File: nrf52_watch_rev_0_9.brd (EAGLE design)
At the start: 31 x 34 mm, 25 parts, among them IC1 HOLYIOT_18010, IC2 MX25R6435FM2IL0, IC4 MMA8652FCR1, J1 0528921033

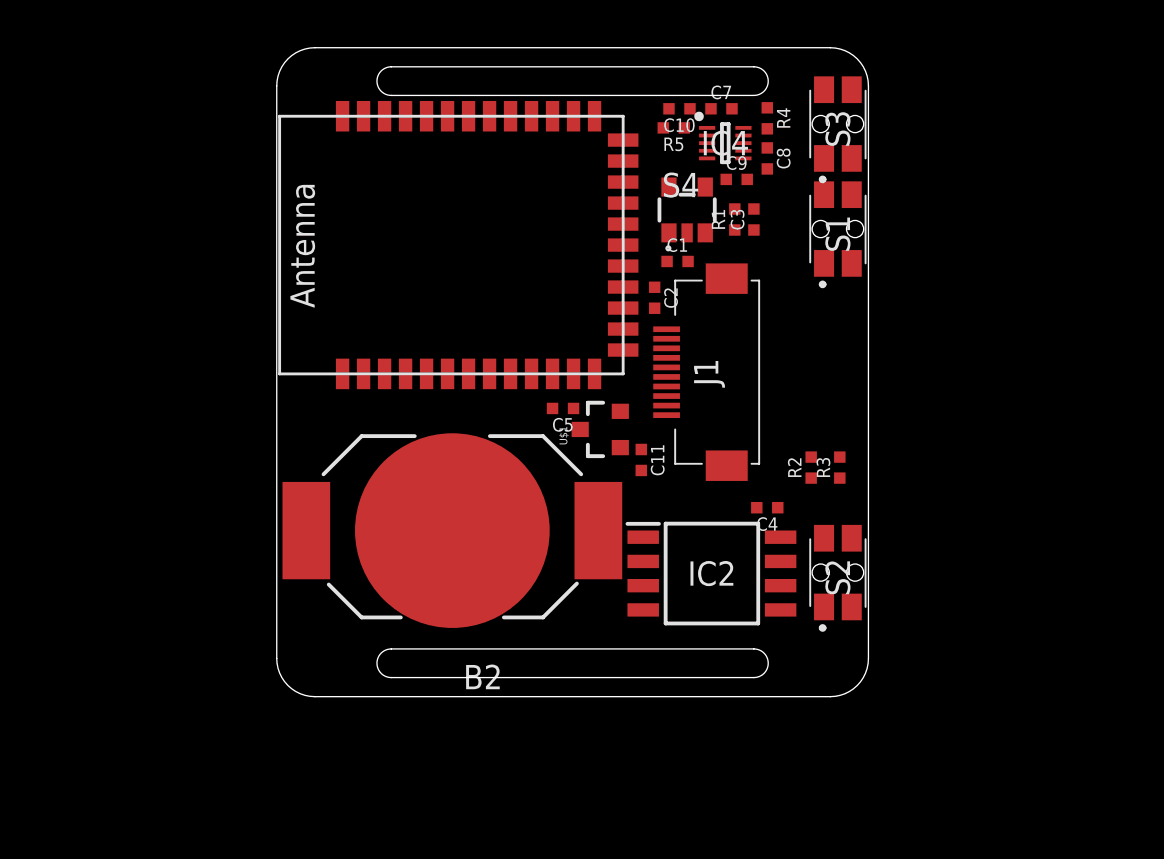
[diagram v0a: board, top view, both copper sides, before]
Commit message: first draft of routing done
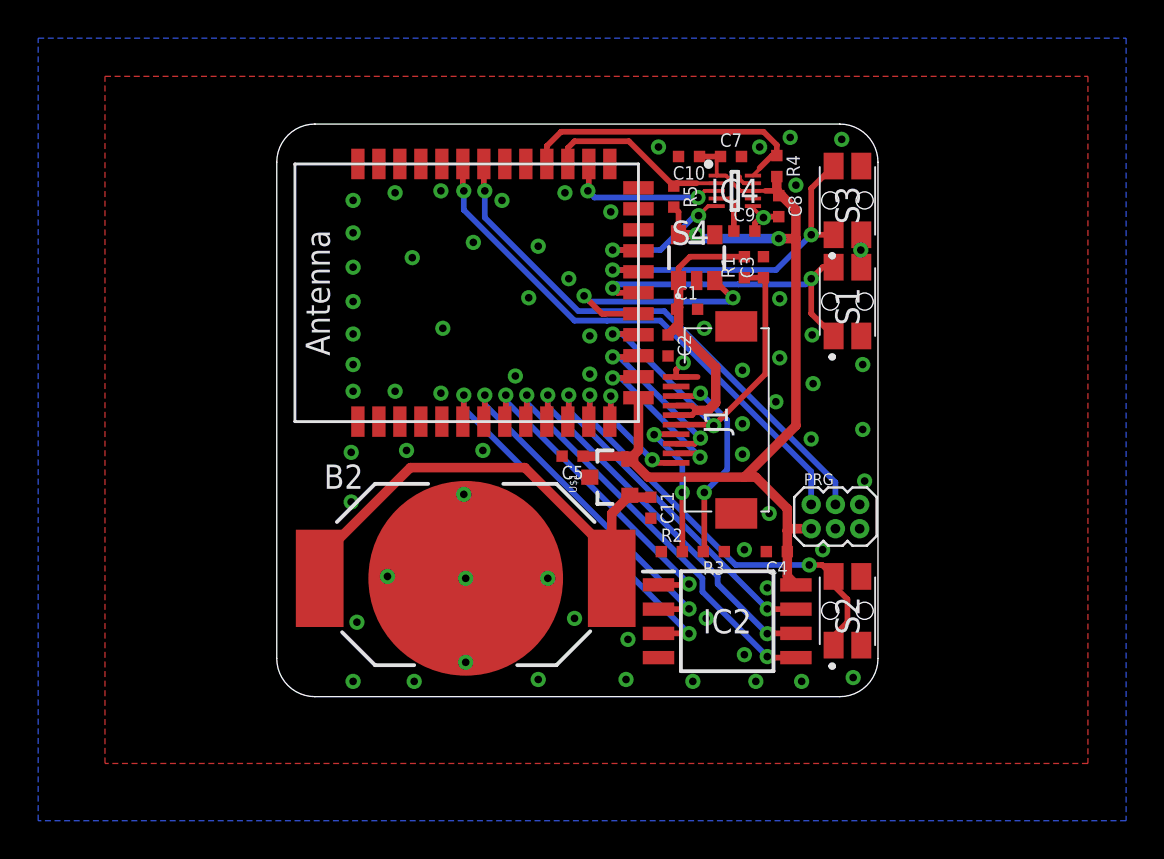
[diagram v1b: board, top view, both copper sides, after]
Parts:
- added PRG: NO_BOM, Inventas-Connectors:1X06_1.27MM
- moved R2 8.52 mm to (20.7, 7.60), turned to 0 degrees
- moved R3 7.93 mm to (22.9, 7.60), turned to 180 degrees
- moved S3 4.03 mm to (29.9, 26.0)
- moved S1 3.83 mm to (29.9, 20.7)
- moved R5 3.60 mm to (20.8, 26.2), turned to 270 degrees
- moved C9 2.73 mm to (24.5, 24.4)
- moved IC2 2.62 mm to (23.6, 3.95)
- moved IC1 2.62 mm to (9.95, 21.2)
- moved C2 2.60 mm to (20.5, 18.4)
- moved B2 2.60 mm to (9.90, 6.20)
- moved C8 2.57 mm to (26.3, 25.7)
- moved C1 2.55 mm to (21.5, 20.3)
- moved C10 2.55 mm to (21.6, 28.3)
- moved C11 2.55 mm to (19.6, 9.90)
- moved C3 2.55 mm to (25.5, 22.5)
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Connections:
- net ACC_INT1: now also IC1.26
- net ACC_INT2: now also IC1.21
- net BTN_BOTTOM: now also IC1.12
- net BTN_MID: now also IC1.19
- net BTN_TOP: now also IC1.20
- net GND: now also PRG.5
- net I2C_SCL: now also IC1.27
- net I2C_SDA: now also IC1.28
- net LCD_DISP: now also IC1.17
- net LCD_POWER_CONTROL: now also IC1.18
- net LCD_SCLK: now also IC1.13
- net LCD_SCS: now also IC1.16
- net LCD_SI: now also IC1.15
- net QSPI_CS: now also IC1.8
- net QSPI_SCLK: now also IC1.10
- net QSPI_SIO0: now also IC1.9
- net QSPI_SIO1: now also IC1.7
- net QSPI_SIO2: now also IC1.6
- net QSPI_SIO3: now also IC1.11
- net SWDCLK: now also PRG.4
- net SWDIO: now also PRG.2
- net VDD: now also PRG.1
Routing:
- net VDD: track 0.00 -> 51.6 mm, vias 0 -> 2
- net SWDCLK: track 0.00 -> 28.1 mm, vias 0 -> 1
- net SWDIO: track 0.00 -> 28.0 mm, vias 0 -> 1
- net N$1: track 0.00 -> 27.4 mm
- net BTN_BOTTOM: track 0.00 -> 23.1 mm, vias 0 -> 2
- net QSPI_SIO0: track 0.00 -> 21.9 mm, vias 0 -> 2
- net LCD_DISP: track 0.00 -> 20.6 mm, vias 0 -> 2
- net QSPI_SIO2: track 0.00 -> 20.4 mm, vias 0 -> 2
- net QSPI_SCLK: track 0.00 -> 20.2 mm, vias 0 -> 2
- net QSPI_SIO1: track 0.00 -> 18.6 mm, vias 0 -> 2
- net QSPI_SIO3: track 0.00 -> 18.4 mm, vias 0 -> 2
- net BTN_TOP: track 0.00 -> 17.8 mm, vias 0 -> 2
- net BTN_MID: track 0.00 -> 17.0 mm, vias 0 -> 2
- net QSPI_CS: track 0.00 -> 16.9 mm, vias 0 -> 2
- net LCD_POWER: track 0.00 -> 15.9 mm
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- added copper zone on layer 1, net GND
- added copper zone on layer 16, net GND
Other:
- board size 31 x 34 mm -> 31.5 x 30 mm

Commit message: changes to rouing. Added batter voltage measure. Added mounting holes
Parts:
- added C6: 10nF, Inventas-Passives:C0402
- added R7: 4M, Inventas-Passives:R0402
- added R8: 10M, Inventas-Passives:R0402
- moved C10 6.11 mm to (27.3, 26.1), turned to 90 degrees
- moved R5 0.40 mm to (20.8, 25.8)
- moved S1 0.40 mm to (29.9, 20.3)
- moved S3 0.40 mm to (29.9, 25.6)
- renumbered U$1 to IC5
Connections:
- new net BATT_MEASURE: C6.1, IC1.6, R7.1, R8.2
- net GND: now also C6.2, R8.1
- net N$1: now also R7.2
- net QSPI_SIO2: now also IC1.5; no longer IC1.6
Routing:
- net N$1: track 27.4 -> 36.6 mm
- net BATT_MEASURE: track 0.00 -> 6.68 mm
- net GND: track 5.55 -> 6.95 mm, vias 70 -> 73
- net VDD: track 51.6 -> 50.2 mm
- net QSPI_SIO2: track 20.4 -> 21.1 mm

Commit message: small fixes. all components are now 3D
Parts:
- moved PRG 0.50 mm to (28.0, 8.30)
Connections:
- net GND: now also IC1.22
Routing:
- net SWDIO: track 28.0 -> 28.5 mm
- net SWDCLK: track 28.1 -> 28.6 mm
- net GND: vias 73 -> 72
